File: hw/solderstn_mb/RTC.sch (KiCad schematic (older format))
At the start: 12 parts, among them Q2101 AO3401A, Q2102 DMG1013T, U2101 DS3231M, U2102 CAT24C256, U2103 DS3231MZ

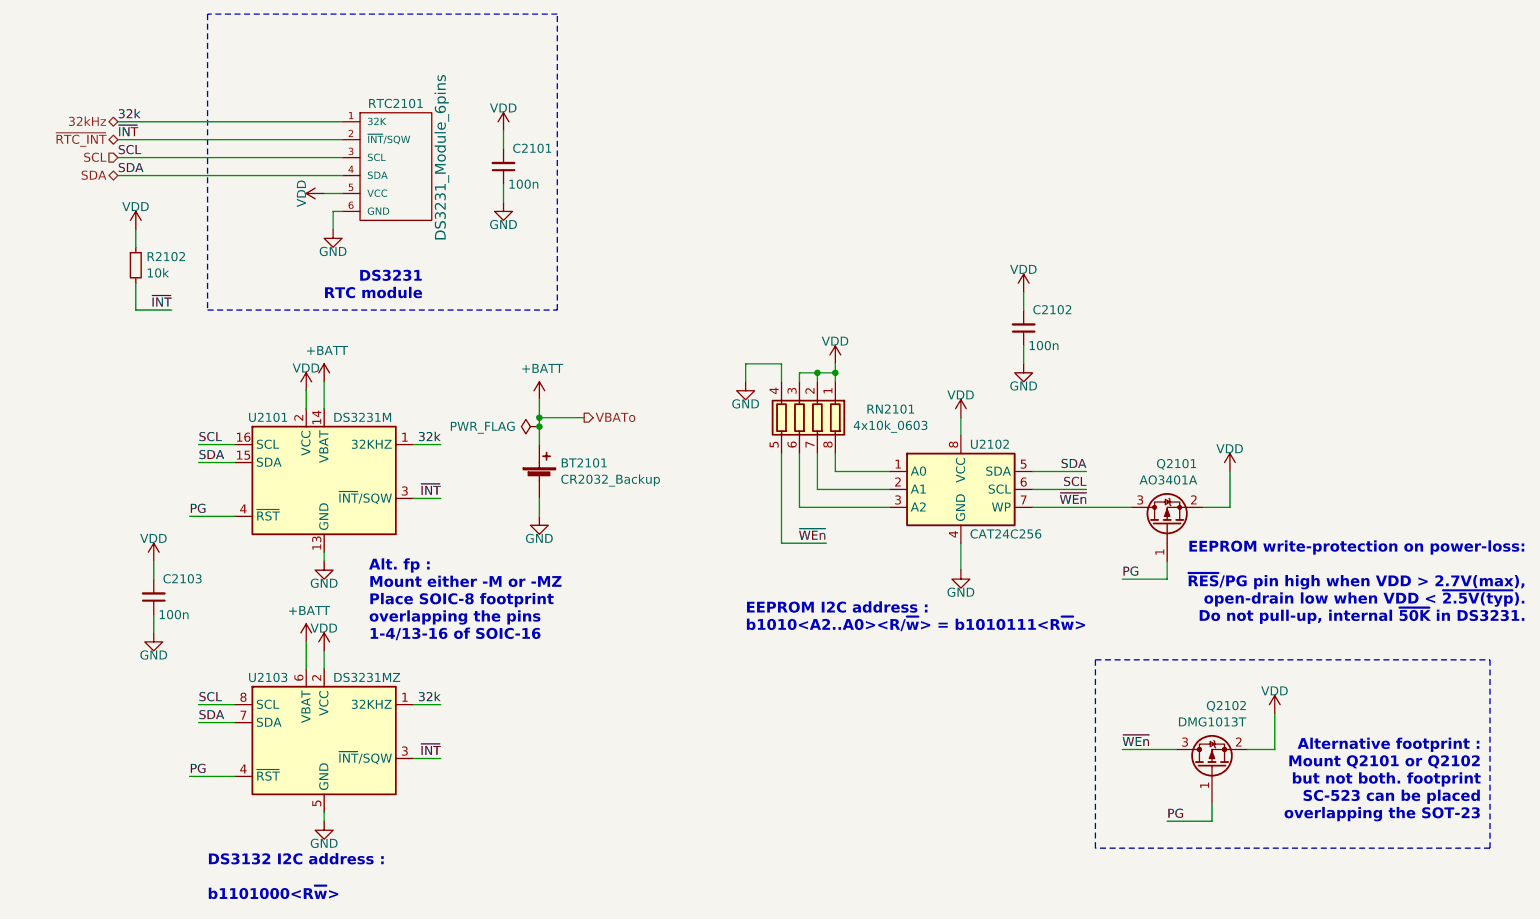
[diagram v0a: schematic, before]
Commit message: MB: major update of footprints, LCSC part numbers and Basic/Extended library indicator, for _most_ of the BoM. (Also removed JP1101/JP1102, bypass jmprs)
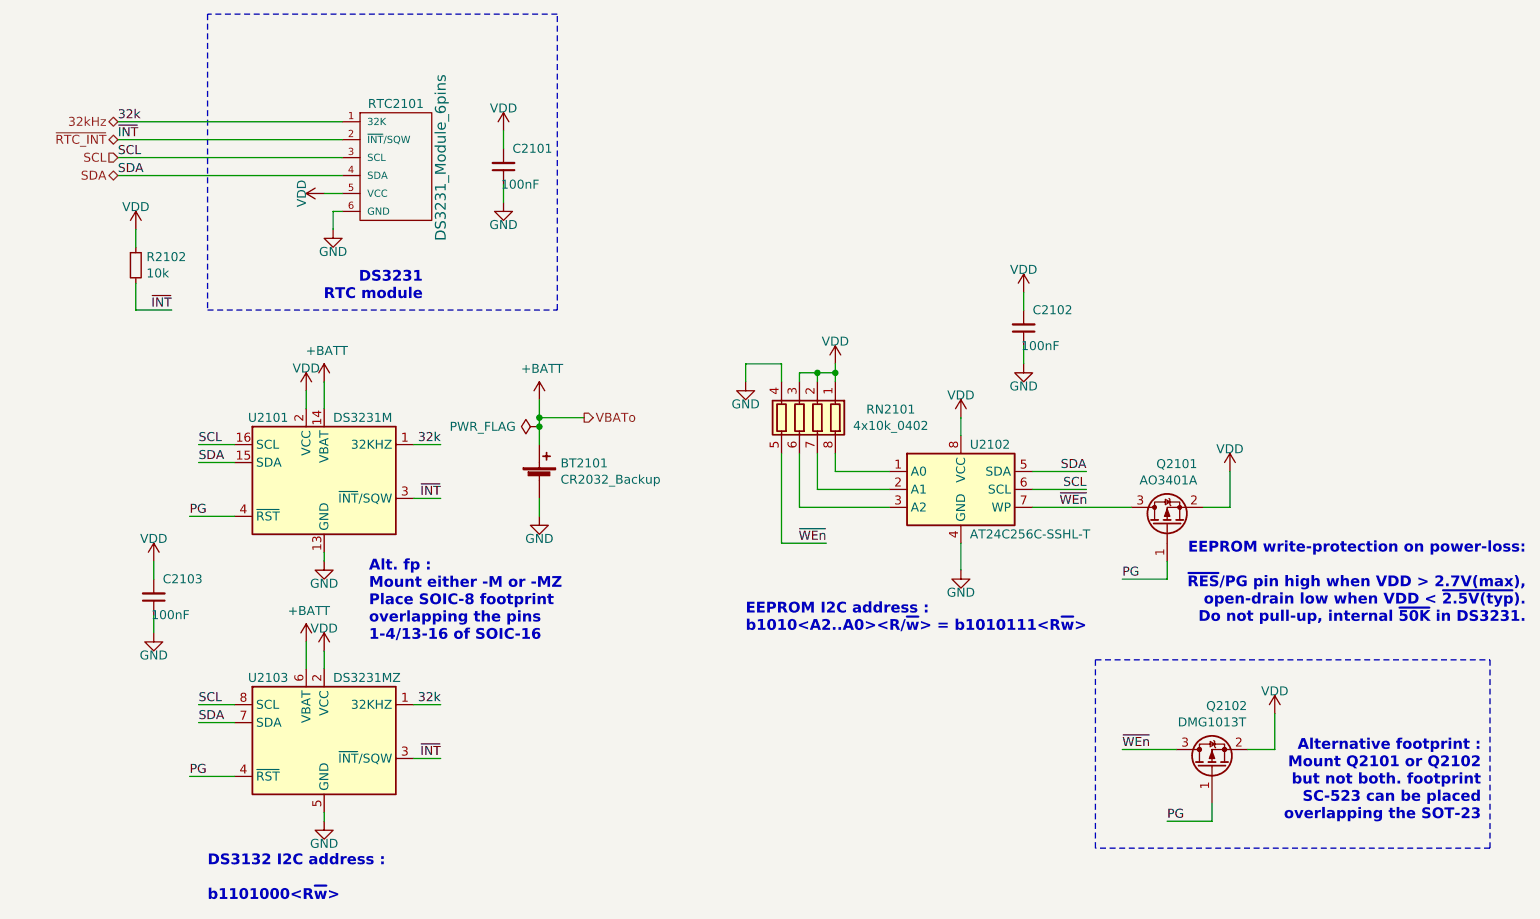
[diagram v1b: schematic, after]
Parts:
- C2101, C2102, C2103: value 100n -> 100nF; footprint Capacitor_SMD:C_0603_1608Metric -> Capacitor_SMD:C_0402_1005Metric; JLC_part (none) -> Basic; LCSC (none) -> C1525
- Q2101: JLC_part (none) -> Basic; LCSC (none) -> C15127
- Q2102: footprint bobs:SOT-523 -> customlib_mj_fp:SOT-523_handsoldering; JLC_part (none) -> Extended; LCSC (none) -> C96676
- R2102: JLC_part (none) -> Basic; LCSC (none) -> C25744
- RN2101: value 4x10k_0603 -> 4x10k_0402; footprint Resistor_SMD:R_Array_Convex_4x0603 -> Resistor_SMD:R_Array_Convex_4x0402; JLC_part (none) -> Basic; LCSC (none) -> C25725
- U2101: JLC_part (none) -> Basic; LCSC (none) -> C37663
- U2102: value CAT24C256 -> AT24C256C-SSHL-T; JLC_part (none) -> Basic; LCSC (none) -> C6482
- U2103: JLC_part (none) -> Extended; LCSC (none) -> C107410
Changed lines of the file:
@@
 AR Path="/5EACD927/5FB940E3/5FBA1629" Ref="C2101"  Part="1"
 F 0 "C2101" H 3900 2100 50  0000 R CNN
-F 1 "100n" H 3750 2300 50  0000 L CNN
-F 2 "Capacitor_SMD:C_0603_1608Metric" H 3950 2200 50  0001 C CNN
+F 1 "100nF" H 3750 2300 50  0000 L CNN
+F 2 "Capacitor_SMD:C_0402_1005Metric" H 3950 2200 50  0001 C CNN
 F 3 "~" H 3950 2200 50  0001 C CNN
+F 4 "Basic" H 3950 2200 50  0001 C CNN "JLC_part"
+F 5 "C1525" H 3950 2200 50  0001 C CNN "LCSC"
 	1    3950 2200
 	-1   0    0    1
@@
 F 2 "Package_SO:SOIC-16W_7.5x10.3mm_P1.27mm" H 2950 3350 50  0001 C CNN
 F 3 "http://datasheets.maximintegrated.com/en/ds/DS3231.pdf" H 3220 4000 50  0001 C CNN
+F 4 "Basic" H 2950 3950 50  0001 C CNN "JLC_part"
+F 5 "C37663" H 2950 3950 50  0001 C CNN "LCSC"
 	1    2950 3950
 	1    0    0    -1
@@
 F 2 "Package_SO:SOIC-8_3.9x4.9mm_P1.27mm" H 2950 4900 50  0001 C CNN
 F 3 "http://datasheets.maximintegrated.com/en/ds/DS3231M.pdf" H 2950 4800 50  0001 C CNN
+F 4 "Extended" H 2950 5400 50  0001 C CNN "JLC_part"
+F 5 "C107410" H 2950 5400 50  0001 C CNN "LCSC"
 	1    2950 5400
 	1    0    0    -1
@@
 AR Path="/5EACD927/5FB940E3/5FBB8034" Ref="C2103"  Part="1"
 F 0 "C2103" H 1950 4500 50  0000 R CNN
-F 1 "100n" H 1800 4700 50  0000 L CNN
-F 2 "Capacitor_SMD:C_0603_1608Metric" H 2000 4600 50  0001 C CNN
+F 1 "100nF" H 1800 4700 50  0000 L CNN
+F 2 "Capacitor_SMD:C_0402_1005Metric" H 2000 4600 50  0001 C CNN
 F 3 "~" H 2000 4600 50  0001 C CNN
+F 4 "Basic" H 2000 4600 50  0001 C CNN "JLC_part"
+F 5 "C1525" H 2000 4600 50  0001 C CNN "LCSC"
 	1    2000 4600
 	-1   0    0    1
@@
 P 6500 4000
 F 0 "U2102" H 6550 4250 50  0000 L CNN
-F 1 "CAT24C256" H 6550 3750 50  0000 L CNN
+F 1 "AT24C256C-SSHL-T" H 6550 3750 50  0000 L CNN
 F 2 "Package_SO:SO-8_3.9x4.9mm_P1.27mm" H 6500 4000 50  0001 C CNN
 F 3 "https://www.onsemi.cn/PowerSolutions/document/CAT24C256-D.PDF" H 6500 4000 50  0001 C CNN
+F 4 "Basic" H 6500 4000 50  0001 C CNN "JLC_part"
+F 5 "C6482" H 6500 4000 50  0001 C CNN "LCSC"
 	1    6500 4000
 	1    0    0    -1
@@
 AR Path="/5EACD927/5FB940E3/5FBC605A" Ref="C2102"  Part="1"
 F 0 "C2102" H 6800 3000 50  0000 R CNN
-F 1 "100n" H 6650 3200 50  0000 L CNN
-F 2 "Capacitor_SMD:C_0603_1608Metric" H 6850 3100 50  0001 C CNN
+F 1 "100nF" H 6650 3200 50  0000 L CNN
+F 2 "Capacitor_SMD:C_0402_1005Metric" H 6850 3100 50  0001 C CNN
 F 3 "~" H 6850 3100 50  0001 C CNN
+F 4 "Basic" H 6850 3100 50  0001 C CNN "JLC_part"
+F 5 "C1525" H 6850 3100 50  0001 C CNN "LCSC"
 	1    6850 3100
 	-1   0    0    1
@@
 F 2 "Package_TO_SOT_SMD:SOT-23" H 7850 4125 50  0001 L CIN
 F 3 "http://www.aosmd.com/pdfs/datasheet/AO3401A.pdf" H 7650 4200 50  0001 L CNN
+F 4 "Basic" H 7650 4200 50  0001 C CNN "JLC_part"
+F 5 "C15127" H 7650 4200 50  0001 C CNN "LCSC"
 	1    7650 4200
 	0    -1   -1   0
@@
 F 0 "Q2102" V 8243 5354 50  0000 L CNN
 F 1 "DMG1013T" V 8152 5550 50  0000 C CNN
-F 2 "bobs:SOT-523" H 8100 5650 50  0001 C CNN
+F 2 "customlib_mj_fp:SOT-523_handsoldering" H 8100 5650 50  0001 C CNN
 F 3 "https://www.diodes.com/assets/Datasheets/ds31784.pdf" H 7900 5550 50  0001 C CNN
+F 4 "Extended" H 7900 5550 50  0001 C CNN "JLC_part"
+F 5 "C96676" H 7900 5550 50  0001 C CNN "LCSC"
 	1    7900 5550
 	0    -1   -1   0
@@
 P 5600 3600
 F 0 "RN2101" H 5091 3554 50  0000 C CNN
-F 1 "4x10k_0603" H 5091 3645 50  0000 C CNN
-F 2 "Resistor_SMD:R_Array_Convex_4x0603" V 5875 3600 50  0001 C CNN
+F 1 "4x10k_0402" H 5091 3645 50  0000 C CNN
+F 2 "Resistor_SMD:R_Array_Convex_4x0402" V 5875 3600 50  0001 C CNN
 F 3 "~" H 5600 3600 50  0001 C CNN
+F 4 "Basic" H 5600 3600 50  0001 C CNN "JLC_part"
+F 5 "C25725" H 5600 3600 50  0001 C CNN "LCSC"
 	1    5600 3600
 	-1   0    0    1
@@
 F 2 "Resistor_SMD:R_0402_1005Metric" H 1900 2750 50  0001 C CNN
 F 3 "~" H 1900 2750 50  0001 C CNN
+F 4 "Basic" H 1900 2750 50  0001 C CNN "JLC_part"
+F 5 "C25744" H 1900 2750 50  0001 C CNN "LCSC"
 	1    1900 2750
 	1    0    0    -1
